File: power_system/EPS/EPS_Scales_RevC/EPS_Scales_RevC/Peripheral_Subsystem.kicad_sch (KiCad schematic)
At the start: 44 parts, among them J14 G125-MH11605L3P, U16 INA230

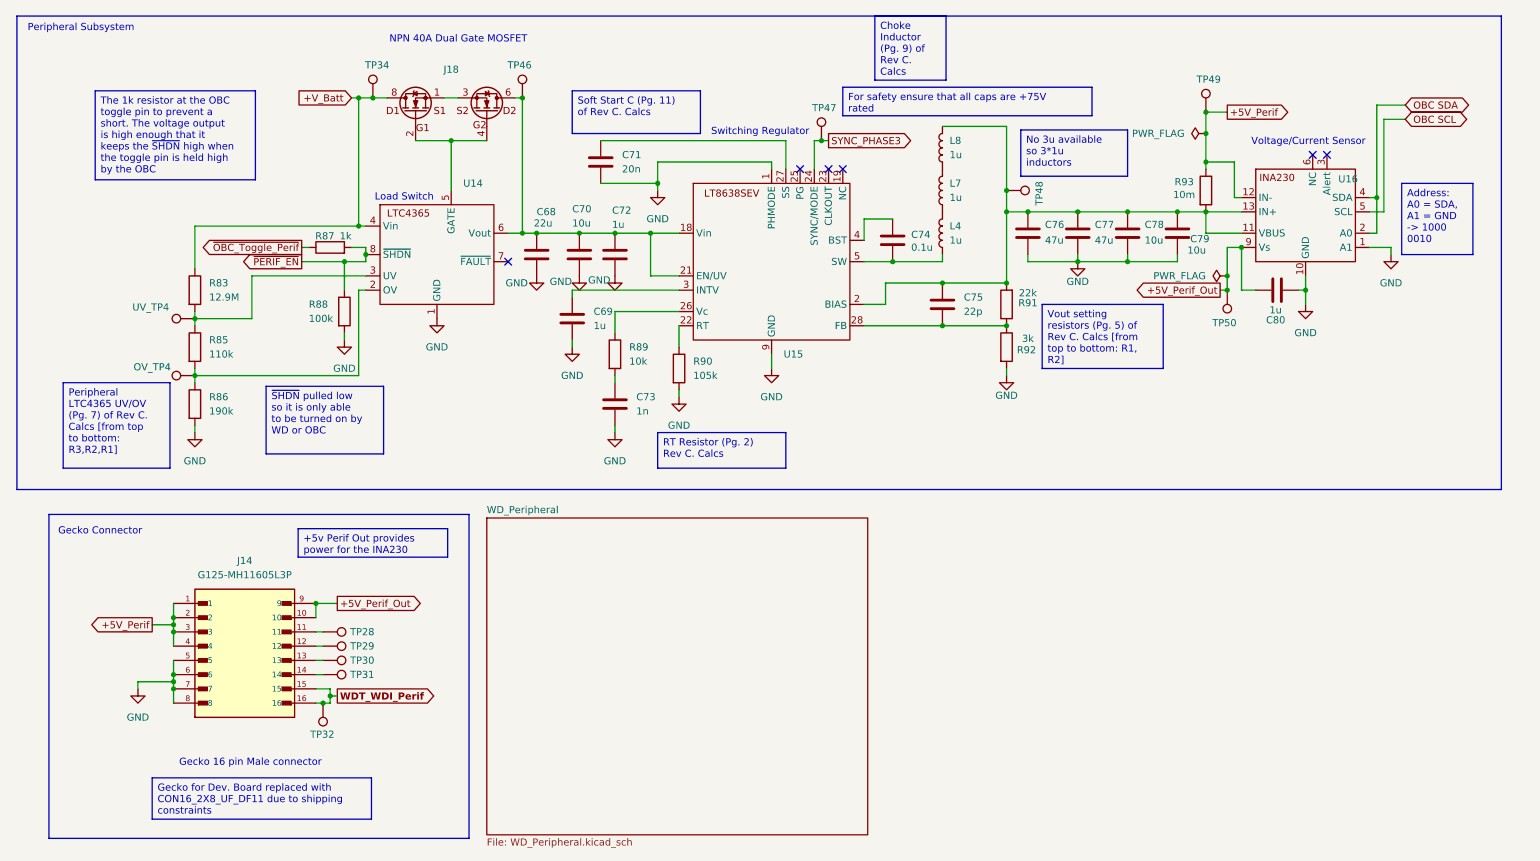
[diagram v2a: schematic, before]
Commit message: Some oopsies but fixed Them, routed one segment
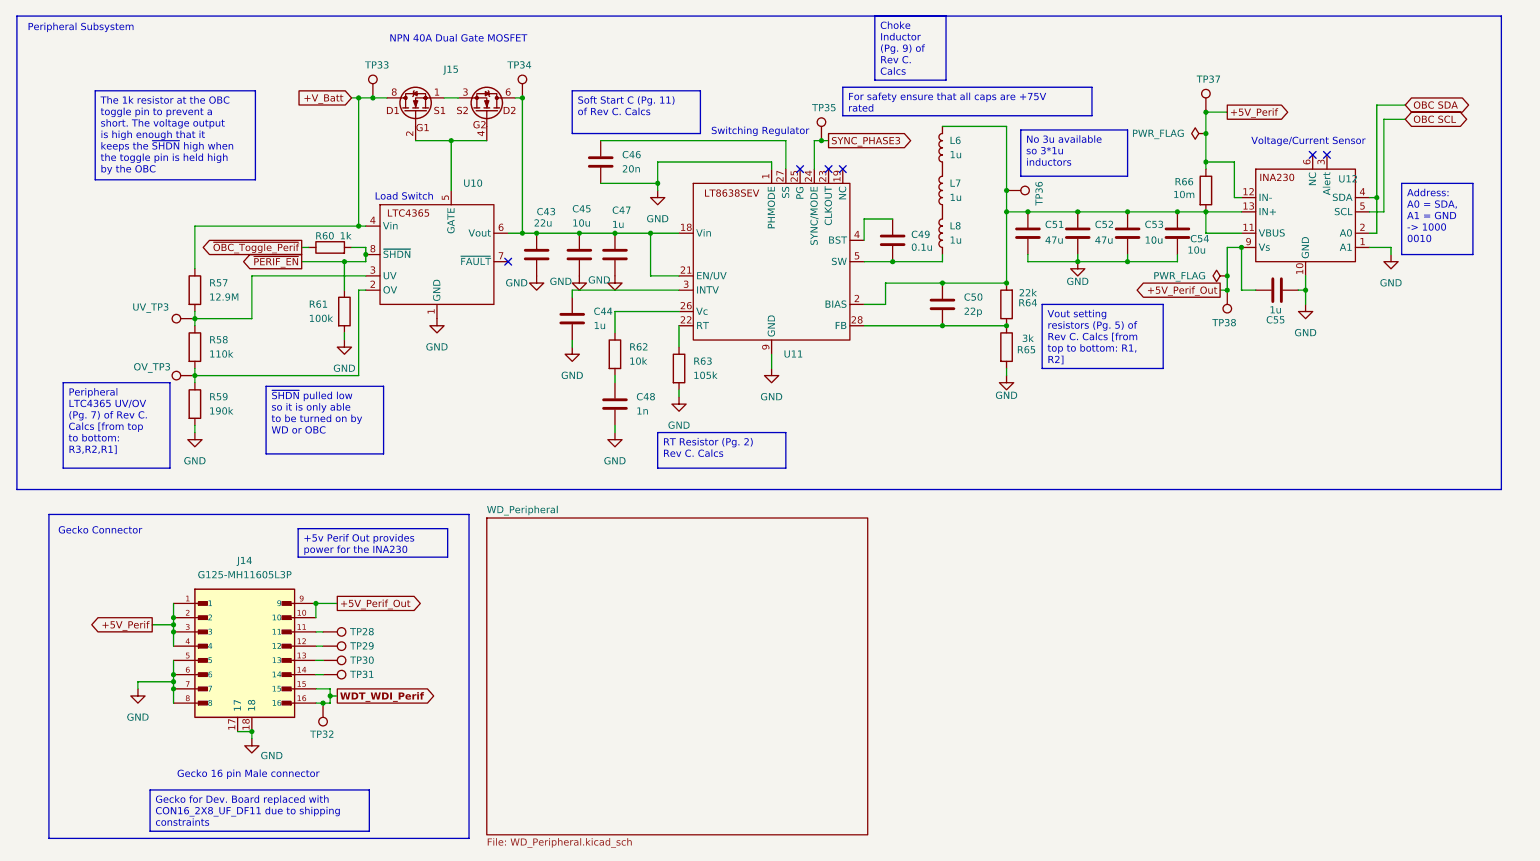
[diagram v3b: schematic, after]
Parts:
- C43: renamed from C68; LCSC (none) -> C309062
- C44: renamed from C69; footprint Capacitor_SMD:C_1210_3225Metric -> Capacitor_SMD:C_0603_1608Metric; LCSC (none) -> C304010
- C46: renamed from C71; footprint Capacitor_SMD:C_1210_3225Metric -> Capacitor_SMD:C_0603_1608Metric; LCSC (none) -> C87721
- C47: renamed from C72; LCSC (none) -> C304010
- C48: renamed from C73; footprint Capacitor_SMD:C_1210_3225Metric -> Capacitor_SMD:C_0603_1608Metric; LCSC (none) -> C2173372
- C49: renamed from C74; LCSC (none) -> C436244
- C55: renamed from C80; LCSC (none) -> C304010
- L6: renamed from L8; LCSC (none) -> C5157561
- L7: LCSC (none) -> C5157561
- L8: renamed from L4; LCSC (none) -> C5157561
- R58: renamed from R85; LCSC (none) -> C25805
- R59: renamed from R86; LCSC (none) -> C25811
- R60: renamed from R87; LCSC (none) -> C13163
- R61: renamed from R88; LCSC (none) -> C14675
- R62: renamed from R89; LCSC (none) -> C13564
- R63: renamed from R90; LCSC (none) -> C16840
- R64: renamed from R91; LCSC (none) -> C23344
- U10: renamed from U14; LCSC (none) -> C580882
- renumbered C70 to C45, C75 to C50, C76 to C51, C77 to C52, C78 to C53, C79 to C54, J18 to J15, OV_TP4 to OV_TP3, R83 to R57, R92 to R65, R93 to R66, TP34 to TP33, TP46 to TP34, TP47 to TP35, TP48 to TP36, TP49 to TP37, TP50 to TP38, U15 to U11, U16 to U12, UV_TP4 to UV_TP3
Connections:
- net GND: now also J14.17, J14.18

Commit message: More Layout Stuff
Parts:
- J15: value ~ -> DN-T1-GE3_VIS; footprint RevC Footprints:SISB46DN-T1-GE3 -> RevC Footprints:MOSFET_DN-T1-GE3_VIS
- U10: value ~ -> LTC4365
- U11: value ~ -> LT8638S
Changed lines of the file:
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@@
 			)
 		)
-		(property "Value" "~"
+		(property "Value" "DN-T1-GE3_VIS"
 			(at 93.98 25.4 0)
 			(effects
@@
 			)
 		)
-		(property "Footprint" "RevC Footprints:SISB46DN-T1-GE3"
+		(property "Footprint" "RevC Footprints:MOSFET_DN-T1-GE3_VIS"
 			(at 93.98 30.48 0)
 			(effects
@@
 		(on_board yes)
 		(dnp no)
-		(fields_autoplaced yes)
 		(property "Reference" "U10"
-			(at 96.1233 44.45 0)
-			(effects
-				(font
-					(size 1.27 1.27)
-				)
-				(justify left)
-			)
-		)
-		(property "Value" "~"
+			(at 97.79 46.736 0)
+			(effects
+				(font
+					(size 1.27 1.27)
+				)
+				(justify left)
+			)
+		)
+		(property "Value" "LTC4365"
 			(at 96.1233 46.99 0)
 			(effects
@@
 		(on_board yes)
 		(dnp no)
-		(fields_autoplaced yes)
 		(property "Reference" "U11"
-			(at 153.2733 74.93 0)
-			(effects
-				(font
-					(size 1.27 1.27)
-				)
-				(justify left)
-			)
-		)
-		(property "Value" "~"
+			(at 137.16 43.434 0)
+			(effects
+				(font
+					(size 1.27 1.27)
+				)
+				(justify left)
+			)
+		)
+		(property "Value" "LT8638S"
 			(at 153.2733 76.2 0)
 			(effects
@@
 		(dnp no)
 		(property "Reference" "U12"
-			(at 252.222 43.688 0)
-			(effects
-				(font
+			(at 237.236 40.894 0)
+			(effects
+				(font

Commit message: Rough Draft of Rev C completed
Still lots of work to do with regards to design constraints, assigning BOM links, and sourcing the components from JLC. Will be doing a deep dive on the PCB subreddit to take notes and learn what I could be missing.
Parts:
- J15: footprint RevC Footprints:MOSFET_DN-T1-GE3_VIS -> RevC Footprints:SISB46DN-T1-GE3
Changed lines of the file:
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@@
 			)
 		)
-		(property "Footprint" "RevC Footprints:MOSFET_DN-T1-GE3_VIS"
+		(property "Footprint" "RevC Footprints:SISB46DN-T1-GE3"
 			(at 93.98 30.48 0)
 			(effects

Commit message: Minor changes to schematic
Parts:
- J14: value G125-MH11605L3P -> CON16_2X8_UF_DF11
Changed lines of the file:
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@@
 			)
 		)
-		(property "Value" "G125-MH11605L3P"
+		(property "Value" "CON16_2X8_UF_DF11"
 			(at 57.15 114.3 0)
 			(effects
@@
 			)
 		)
-		(property "Datasheet" ""
+		(property "Datasheet" "https://www.mouser.com/datasheet/2/185/DF11_26DP_2DS_252852_2529_CL0543_0544_8_52_Catalog-2448894.pdf"
 			(at 57.15 129.54 0)
 			(effects
@@
 			)
 		)
-		(property "Description" ""
+		(property "Description" "Interfacing Connector"
 			(at 57.15 129.54 0)
 			(effects

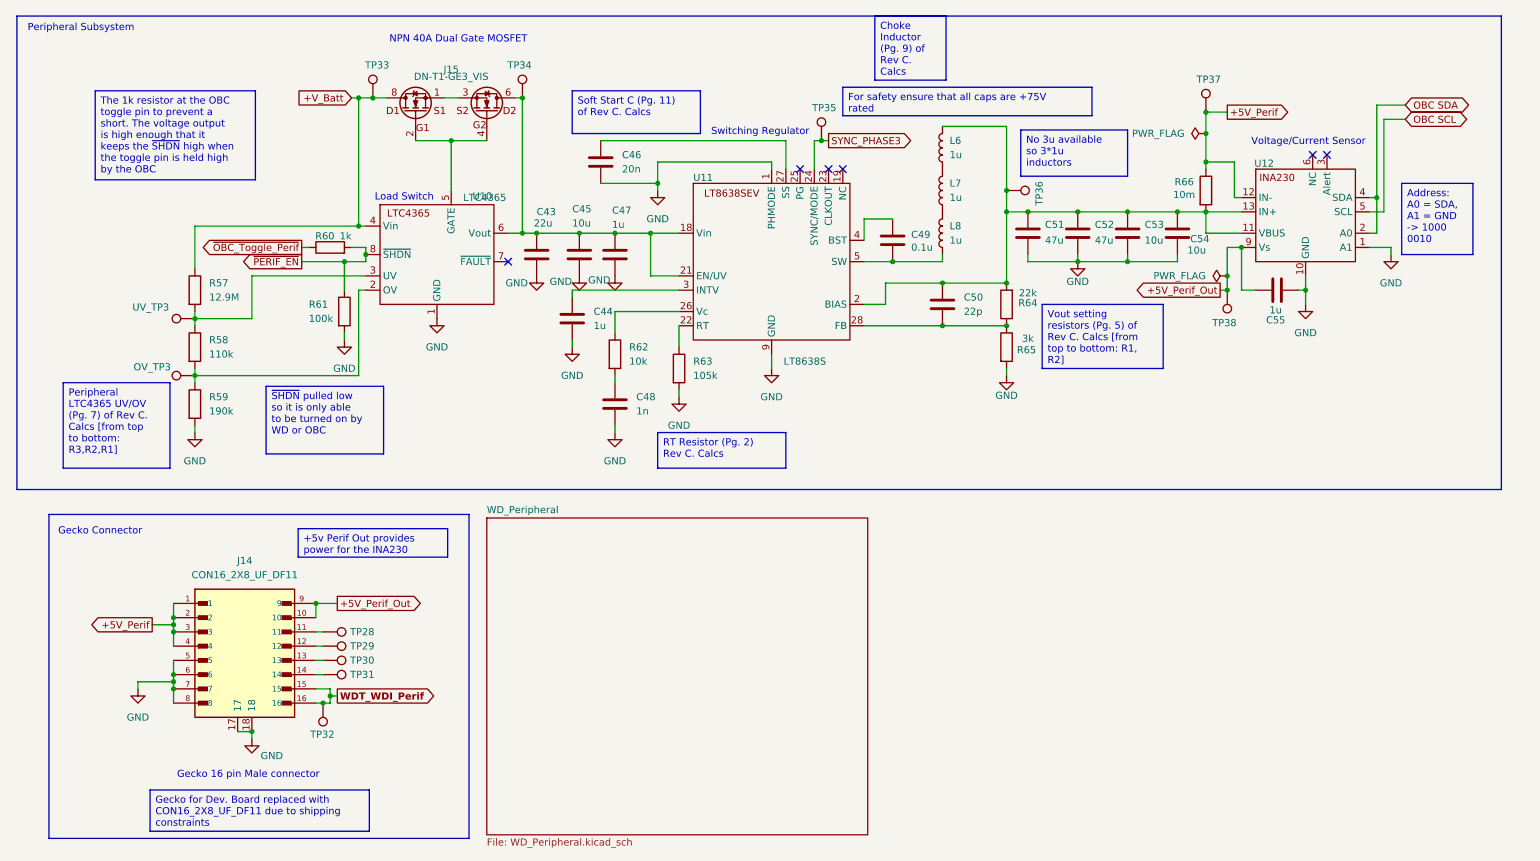
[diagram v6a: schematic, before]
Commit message: Schematic and Layout changes
Made all watch dogs powered by +5v perif supply
All INAs are now powered by the 3.3v OBC supply.
DFU 16 connectors were updated to through hole versions.
Redundant test points were removed.
Layout needs work to reroute new items.
Still need to add I2C buffer
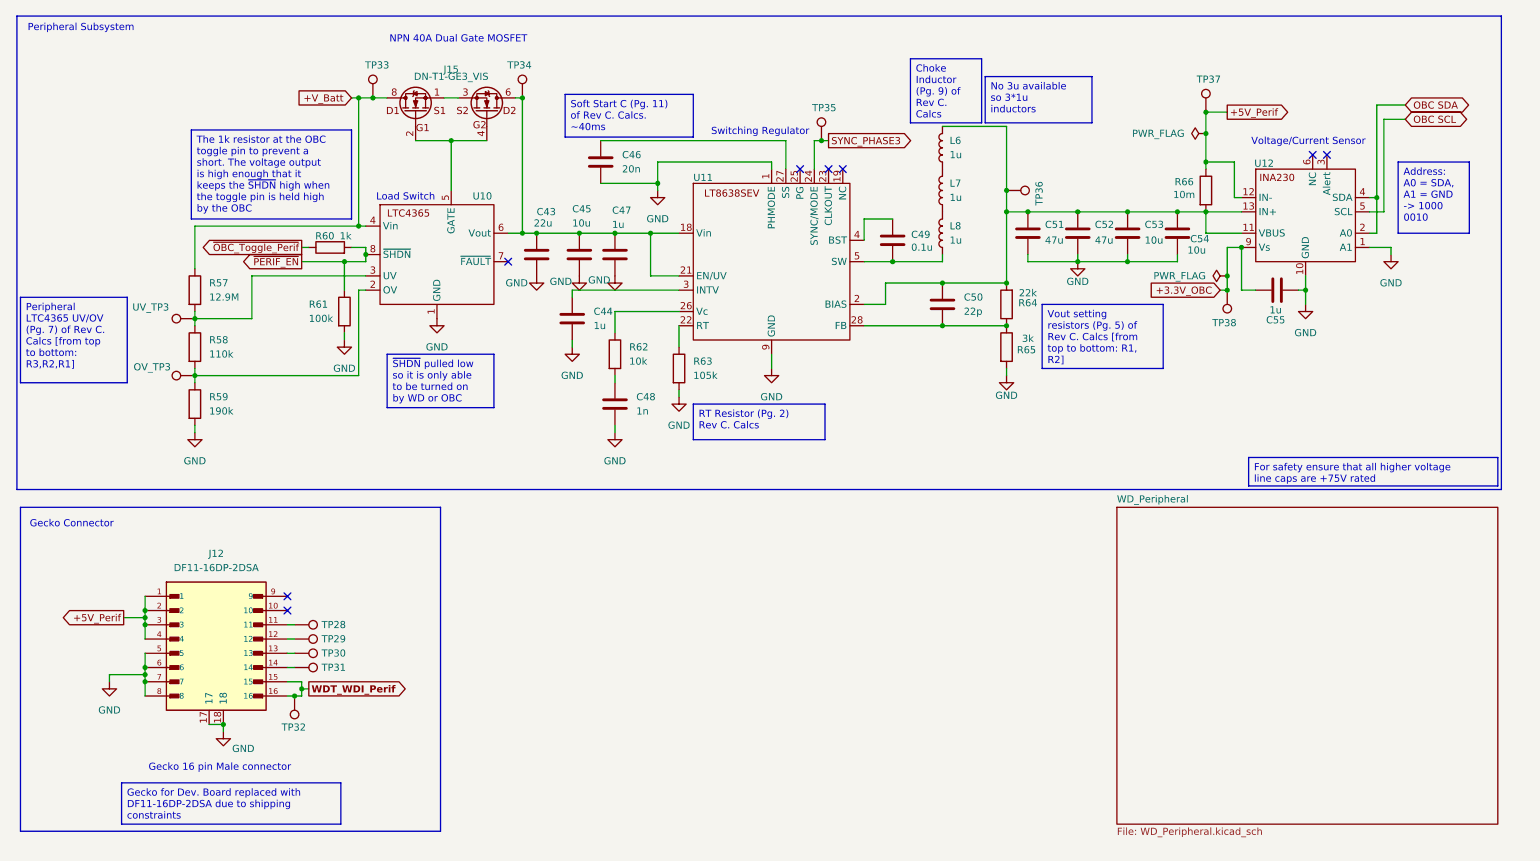
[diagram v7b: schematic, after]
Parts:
- removed J14: CON16_2X8_UF_DF11, RevC Footprints:CON16_2X8_UF_DF11, symbol 16 Pin Gecko Male Connector:G125-MH11605L3P
- added J12: DF11-16DP-2DSA, RevC Footprints:DF1116DP2DSA08, symbol DF11-16DP-2DSA:DF11-16DP-2DSA
- J15: footprint RevC Footprints:SISB46DN-T1-GE3 -> RevC Footprints:MOSFET_DN-T1-GE3_VIS
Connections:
- net +5V_Perif: now also J12.1, J12.2, J12.3, J12.4
- net GND: now also J12.17, J12.18, J12.5, J12.6, J12.7, J12.8
- net WDT_WDI_Perif: now also J12.15, J12.16
- net at TP28.1: now also J12.11
- net at TP30.1: now also J12.13
- net at TP31.1: now also J12.14
- net at TP29.1: now also J12.12
- net +5V_Perif_Out renamed +3.3V_OBC
- no-connect marks 6 -> 8
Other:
- moved on the sheet: TP28, TP29, TP30, TP31, TP32
